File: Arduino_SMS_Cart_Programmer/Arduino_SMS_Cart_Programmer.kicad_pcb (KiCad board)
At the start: 2 copper layers, 60.5 x 75.2 mm, 8 parts, among them J1 SEGA Master System Cartridge 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, U1 74HC595, U2 74HC595

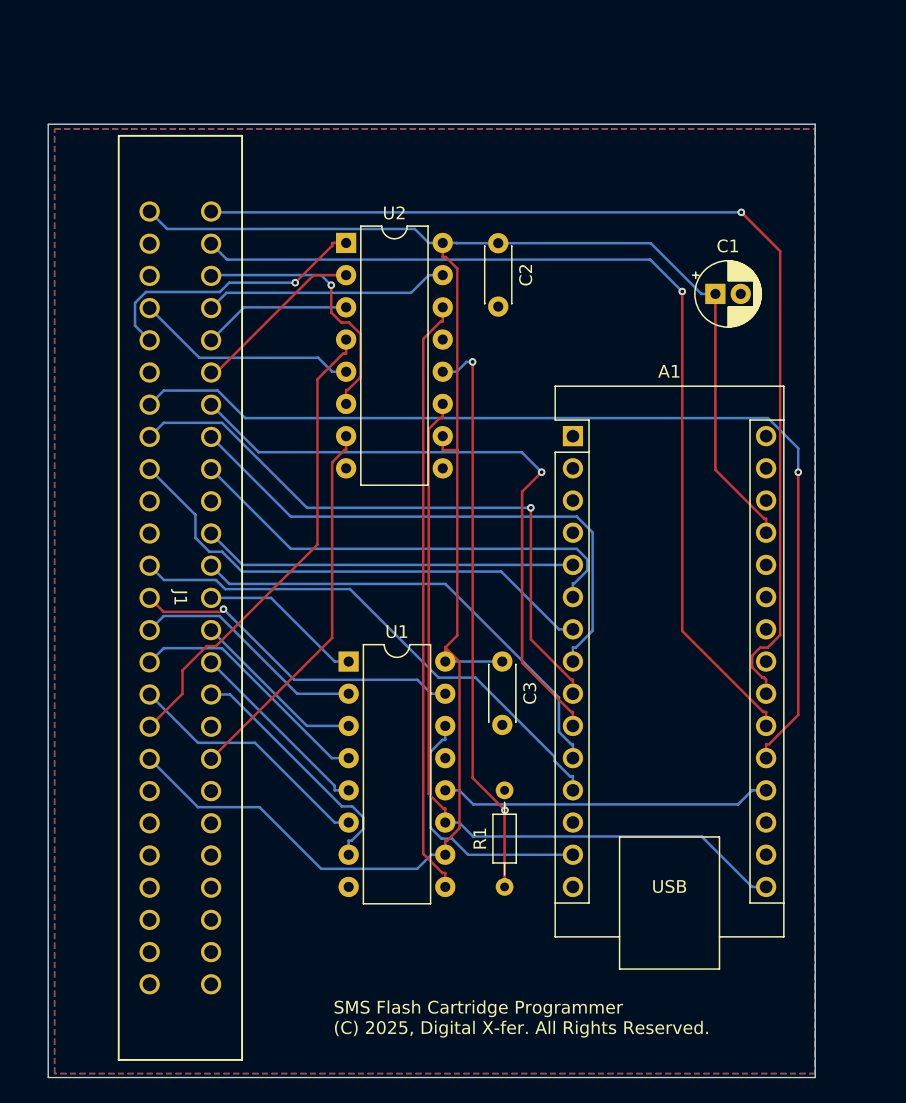
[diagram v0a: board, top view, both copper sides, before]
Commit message: Added cart reset line connection.
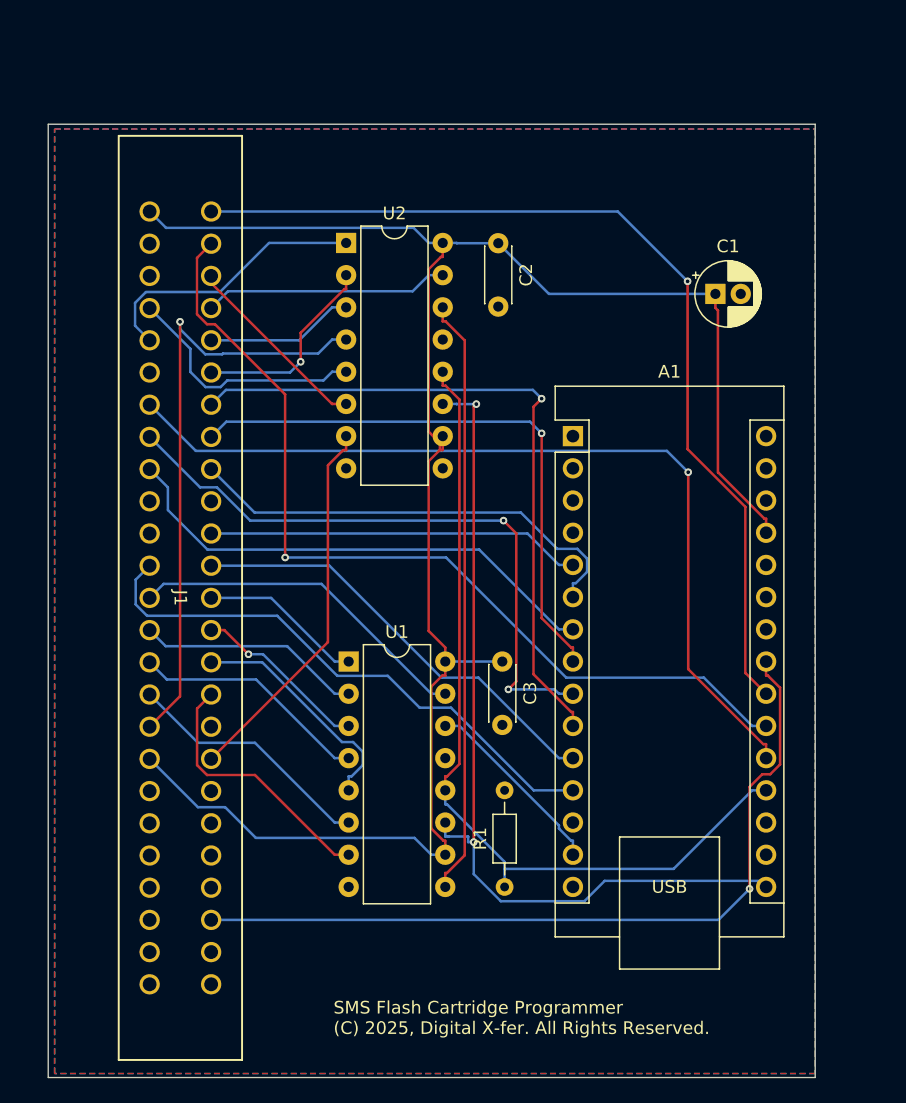
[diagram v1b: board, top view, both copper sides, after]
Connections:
- A1 pad 23: unconnected-(A1-A4-Pad23) -> /RST
- J1 pad 46: unconnected-(J1-Pin_46-Pad46) -> /RST
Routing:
- net /RST: track 0.00 -> 63.3 mm, vias 0 -> 1
- net A12: track 37.5 -> 47.9 mm, vias 0 -> 1
- net /CE: track 79.1 -> 69.9 mm
- net /WR: track 82.8 -> 75.0 mm
- net A14: track 21.0 -> 14.6 mm, vias 1 -> 0
- net SCK: track 61.6 -> 67.7 mm, vias 0 -> 2
- net MOSI: track 20.7 -> 15.1 mm
- net RCLK: track 71.9 -> 67.1 mm, vias 2 -> 0
- net /RD: track 75.9 -> 71.9 mm
- net D7: track 50.7 -> 54.3 mm
- net A5: track 15.2 -> 18.5 mm
- net D1: track 41.6 -> 44.1 mm
- net A10: track 13.4 -> 15.8 mm, vias 0 -> 1
- net D0: track 37.1 -> 34.8 mm
- net A13: track 17.6 -> 19.6 mm
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
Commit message: Added revision to PCB silkscreen.
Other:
- board text added: "SMS Flash Cartridge Programmer Rev B (C) 2025, Digital X-fer. All Rights Reserved."
- board text removed: "SMS Flash Cartridge Programmer (C) 2025, Digital X-fer. All Rights Reserved."
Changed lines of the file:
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@@
 		(layer "Margin")
 	)
-	(gr_text "SMS Flash Cartridge Programmer\n(C) 2025, Digital X-fer. All Rights Reserved."
+	(gr_text "SMS Flash Cartridge Programmer Rev B\n(C) 2025, Digital X-fer. All Rights Reserved."
 		(at 133.5 133 0)
 		(layer "F.SilkS")

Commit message: Added mounting holes and lable to front of cart connector.
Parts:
- added REF**: MountingHole_2.2mm_M2, MountingHole:MountingHole_2.2mm_M2, F.Cu at (168.9, 133.3)
- added REF**: MountingHole_2.2mm_M2, MountingHole:MountingHole_2.2mm_M2, F.Cu at (168.9, 64.1)
- added REF**: MountingHole_2.2mm_M2, MountingHole:MountingHole_2.2mm_M2, F.Cu at (113.7, 64.1)
- added REF**: MountingHole_2.2mm_M2, MountingHole:MountingHole_2.2mm_M2, F.Cu at (113.7, 133.3)
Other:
- board text added: "Front"

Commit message: Cleaned up RevB PCB.
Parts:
- moved REF3 15.7 mm to (126.7, 124.7)
- moved REF1 15.3 mm to (126.7, 56.2)
- moved REF4 11.0 mm to (162.1, 124.7)
- moved REF2 10.5 mm to (162.1, 56.2)
- moved J1 10.1 mm to (124.0, 54.1)
- moved A1 10.1 mm to (146.0, 77.8)
- moved C1 10.1 mm to (157.3, 66.6)
- moved C3 10.1 mm to (140.5, 95.6)
- moved R1 10.1 mm to (140.7, 113.4)
- moved U1 10.1 mm to (128.3, 95.6)
- moved U2 10.1 mm to (128.2, 62.6)
- moved C2 10.1 mm to (140.2, 62.6)
- renumbered REF** to REF1, REF** to REF2, REF** to REF3, REF** to REF4
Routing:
- net D0: track 34.8 -> 70.5 mm
- net D1: track 44.1 -> 56.2 mm, vias 0 -> 1
- net /CE: track 69.9 -> 80.7 mm
- net /WR: track 75.0 -> 82.2 mm
- net A12: track 47.9 -> 40.8 mm
- net SCK: track 67.7 -> 63.3 mm, vias 2 -> 1
- net MOSI: track 15.1 -> 19.3 mm
- net A5: track 18.5 -> 15.2 mm
- net /RD: track 71.9 -> 68.9 mm, vias 1 -> 0
- net A9: track 22.0 -> 19.7 mm
- net A13: track 19.6 -> 21.9 mm
- net /RST: track 63.3 -> 64.9 mm, vias 1 -> 0
- net A10: track 15.8 -> 17.3 mm, vias 1 -> 0
- net RCLK: track 67.1 -> 68.5 mm, vias 0 -> 1
- net VCC: track 150.8 -> 152.2 mm
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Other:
- board size 60.5 x 75.2 mm -> 55.9 x 74.4 mm
- board text added: "SMS Flash Cartridge Programmer (C) 2026, Digital X-fer. All Rights Reserved. Rev-B"
- board text removed: "SMS Flash Cartridge Programmer Rev B (C) 2025, Digital X-fer. All Rights Reserved."
